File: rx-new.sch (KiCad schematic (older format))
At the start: 103 parts, among them J1 RF_IN, J2 PWR, J3 IQ_OUT, J4 4LO_IN, Q1 BC848, Q2 BC858, Q3 BC848, Q4 BC858, U1 TPS79101DBVREP, U2 SN74CBT3253, U3 AD797, U4 AD797, U5 NC7SZ00M5X, U6 OPA1662, U7 74AUP1G74, U8 74AUP1G74

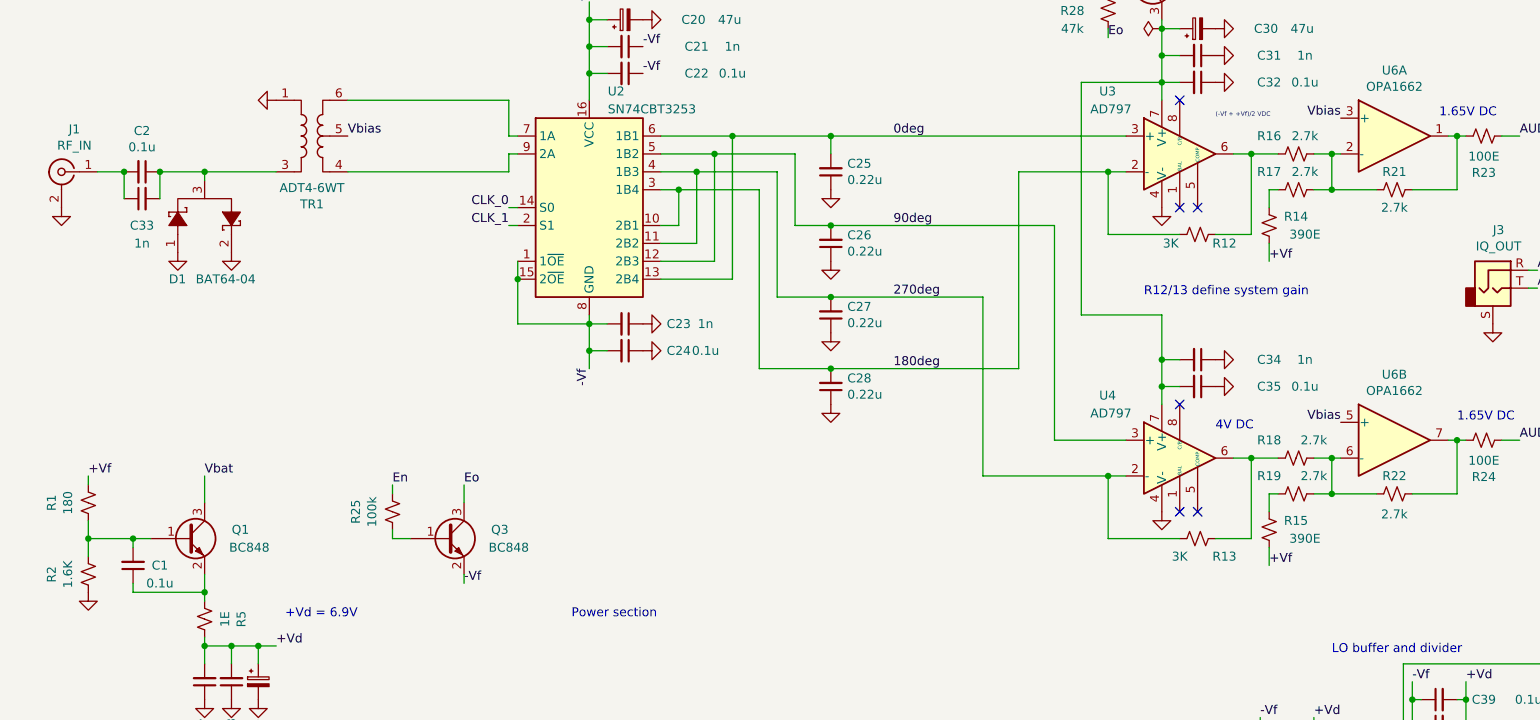
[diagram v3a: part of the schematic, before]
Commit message: Reworked voltages and opamps resistors
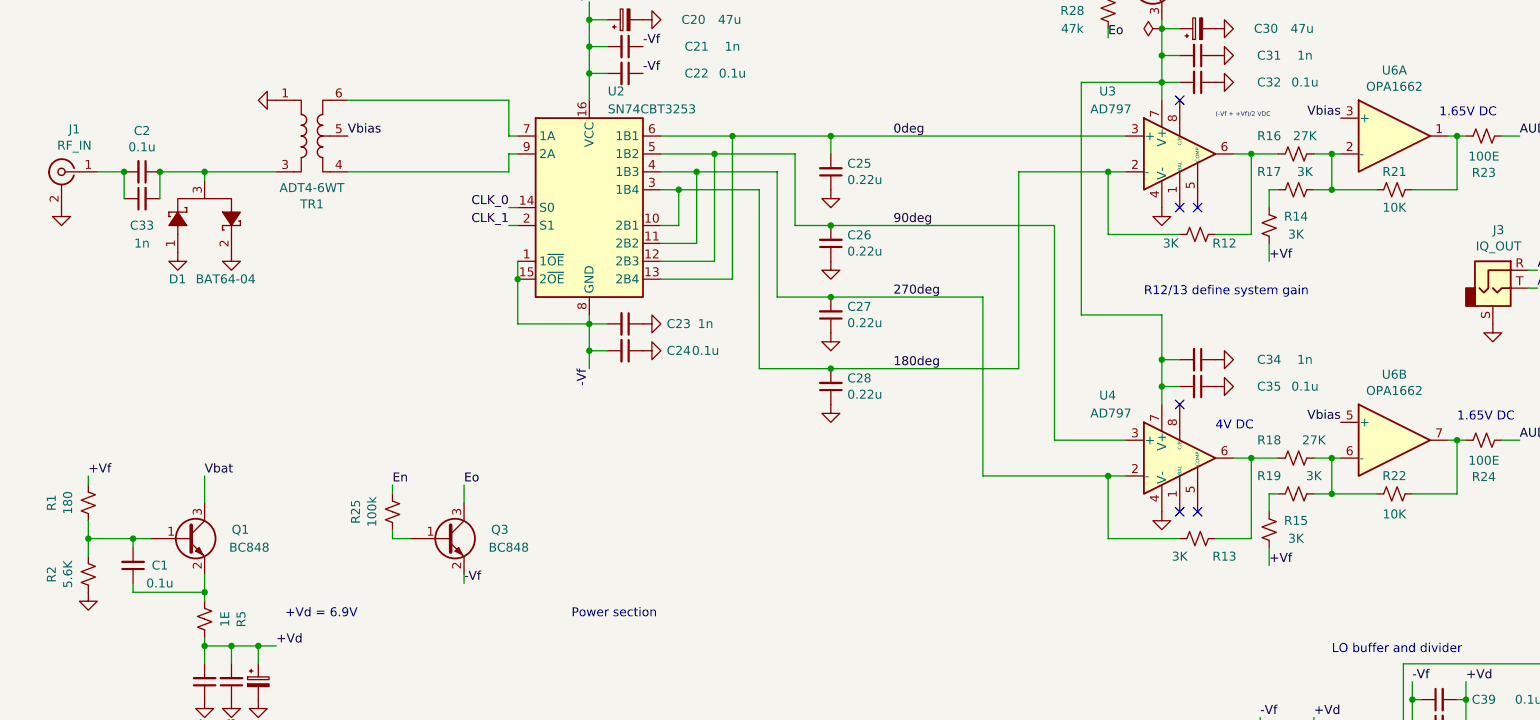
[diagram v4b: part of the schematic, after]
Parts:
- R14, R15: value 390E -> 3K
- R16, R18: value 2.7k -> 27K
- R17, R19: value 2.7k -> 3K
- R2: value 1.6K -> 5.6K
- R21, R22: value 2.7k -> 10K
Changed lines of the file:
@@
 Sheet 1 1
 Title "YO6SSW receiver v2"
-Date "2020-11-13"
-Rev "0.2"
+Date "2020-11-17"
+Rev "0.3"
 Comp "Frédéric Boes, Adrian Scripcă"
 Comment1 ""
@@
 P 1150 4100
 F 0 "R2" V 945 4100 50  0000 C CNN
-F 1 "1.6K" V 1036 4100 50  0000 C CNN
+F 1 "5.6K" V 1036 4100 50  0000 C CNN
 F 2 "Resistor_SMD:R_0805_2012Metric_Pad1.15x1.40mm_HandSolder" H 1150 4100 50  0001 C CNN
 F 3 "~" H 1150 4100 50  0001 C CNN
@@
 P 7900 1750
 F 0 "R16" V 8000 1900 50  0000 C CNN
-F 1 "2.7k" V 8000 1700 50  0000 C CNN
+F 1 "27K" V 8000 1700 50  0000 C CNN
 F 2 "Resistor_SMD:R_0805_2012Metric_Pad1.15x1.40mm_HandSolder" H 7900 1750 50  0001 C CNN
 F 3 "~" H 7900 1750 50  0001 C CNN
@@
 P 7900 1950
 F 0 "R17" V 8000 2100 50  0000 C CNN
-F 1 "2.7k" V 8000 1900 50  0000 C CNN
+F 1 "3K" V 8000 1900 50  0000 C CNN
 F 2 "Resistor_SMD:R_0805_2012Metric_Pad1.15x1.40mm_HandSolder" H 7900 1950 50  0001 C CNN
 F 3 "~" H 7900 1950 50  0001 C CNN
@@
 P 8450 1950
 F 0 "R21" V 8550 1950 50  0000 C CNN
-F 1 "2.7k" V 8350 1950 50  0000 C CNN
+F 1 "10K" V 8350 1950 50  0000 C CNN
 F 2 "Resistor_SMD:R_0805_2012Metric_Pad1.15x1.40mm_HandSolder" H 8450 1950 50  0001 C CNN
 F 3 "~" H 8450 1950 50  0001 C CNN
@@
 P 7750 2150
 F 0 "R14" H 7600 2100 50  0000 C CNN
-F 1 "390E" H 7550 2200 50  0000 C CNN
+F 1 "3K" H 7600 2200 50  0000 C CNN
 F 2 "Resistor_SMD:R_0805_2012Metric_Pad1.15x1.40mm_HandSolder" H 7750 2150 50  0001 C CNN
 F 3 "~" H 7750 2150 50  0001 C CNN
@@
 P 7900 3450
 F 0 "R18" V 8000 3600 50  0000 C CNN
-F 1 "2.7k" V 8000 3350 50  0000 C CNN
+F 1 "27K" V 8000 3350 50  0000 C CNN
 F 2 "Resistor_SMD:R_0805_2012Metric_Pad1.15x1.40mm_HandSolder" H 7900 3450 50  0001 C CNN
 F 3 "~" H 7900 3450 50  0001 C CNN
@@
 P 7900 3650
 F 0 "R19" V 8000 3800 50  0000 C CNN
-F 1 "2.7k" V 8000 3550 50  0000 C CNN
+F 1 "3K" V 8000 3550 50  0000 C CNN
 F 2 "Resistor_SMD:R_0805_2012Metric_Pad1.15x1.40mm_HandSolder" H 7900 3650 50  0001 C CNN
 F 3 "~" H 7900 3650 50  0001 C CNN
@@
 P 8450 3650
 F 0 "R22" V 8550 3650 50  0000 C CNN
-F 1 "2.7k" V 8336 3650 50  0000 C CNN
+F 1 "10K" V 8336 3650 50  0000 C CNN
 F 2 "Resistor_SMD:R_0805_2012Metric_Pad1.15x1.40mm_HandSolder" H 8450 3650 50  0001 C CNN
 F 3 "~" H 8450 3650 50  0001 C CNN
@@
 P 7750 3850
 F 0 "R15" H 7600 3800 50  0000 C CNN
-F 1 "390E" H 7550 3900 50  0000 C CNN
+F 1 "3K" H 7600 3900 50  0000 C CNN
 F 2 "Resistor_SMD:R_0805_2012Metric_Pad1.15x1.40mm_HandSolder" H 7750 3850 50  0001 C CNN
 F 3 "~" H 7750 3850 50  0001 C CNN

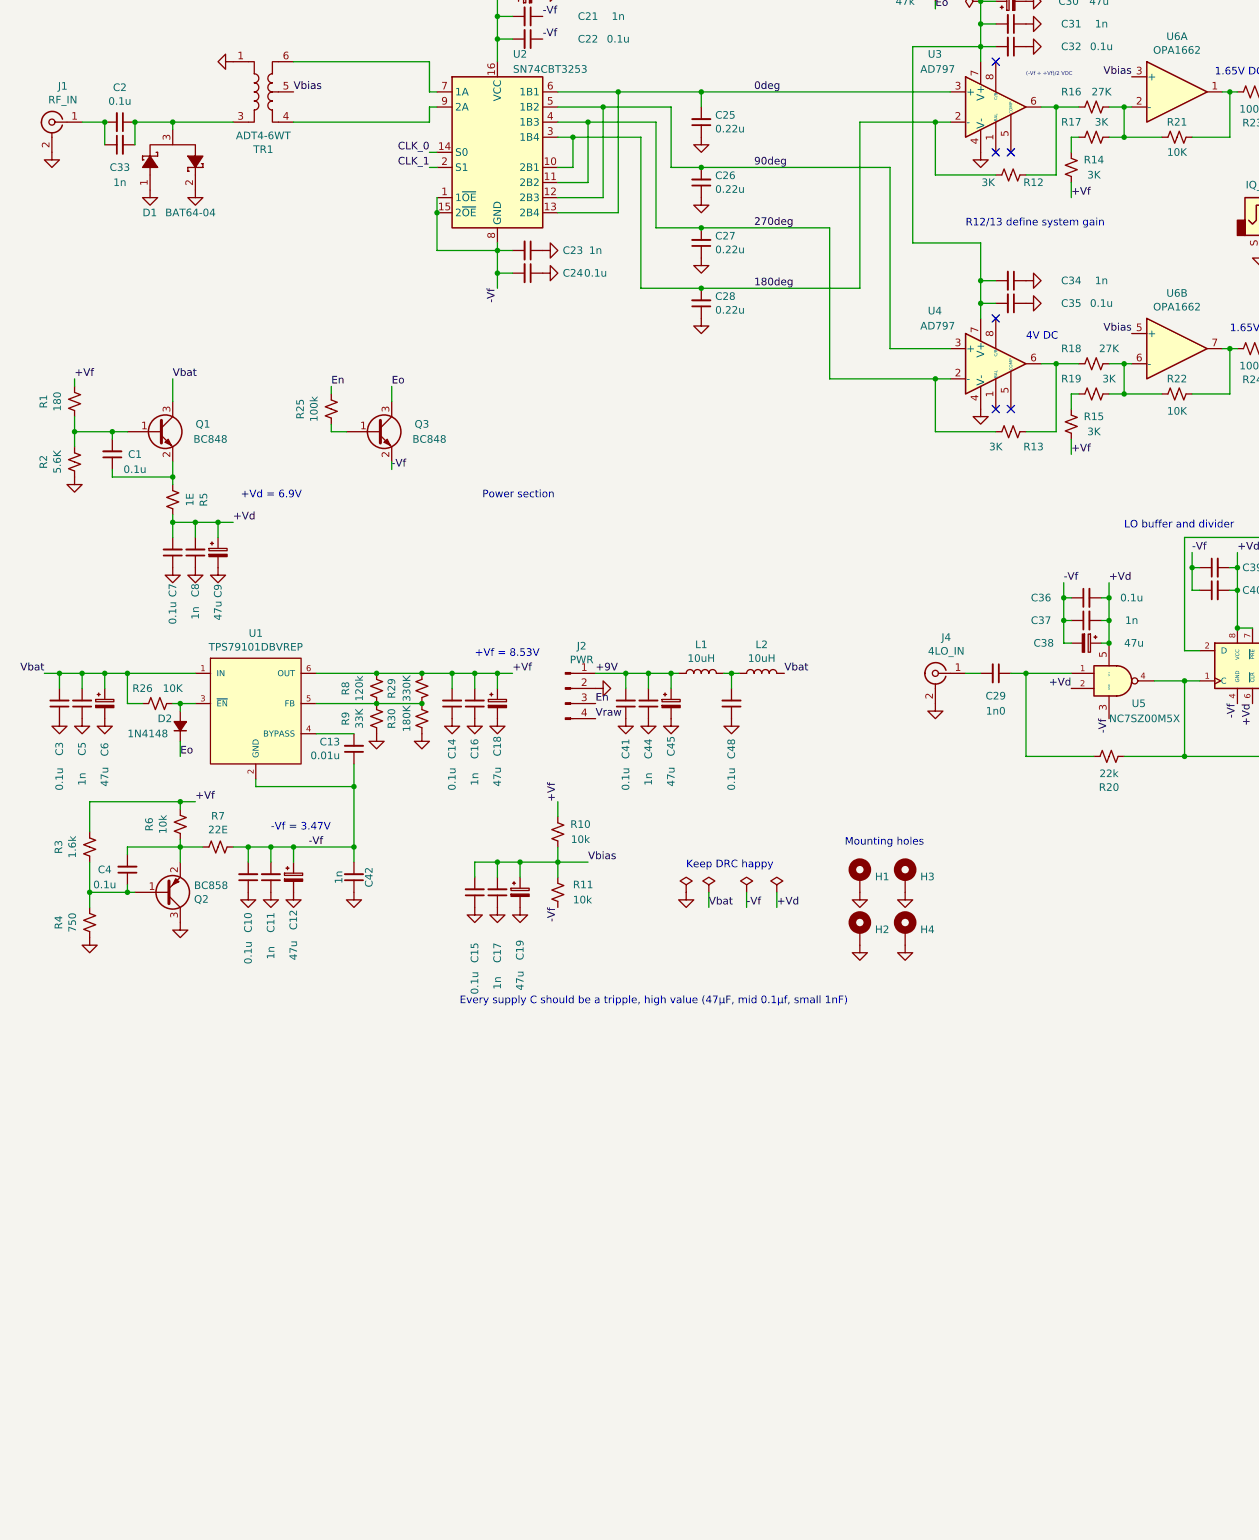
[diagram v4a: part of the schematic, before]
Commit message: Added selectable RX gain
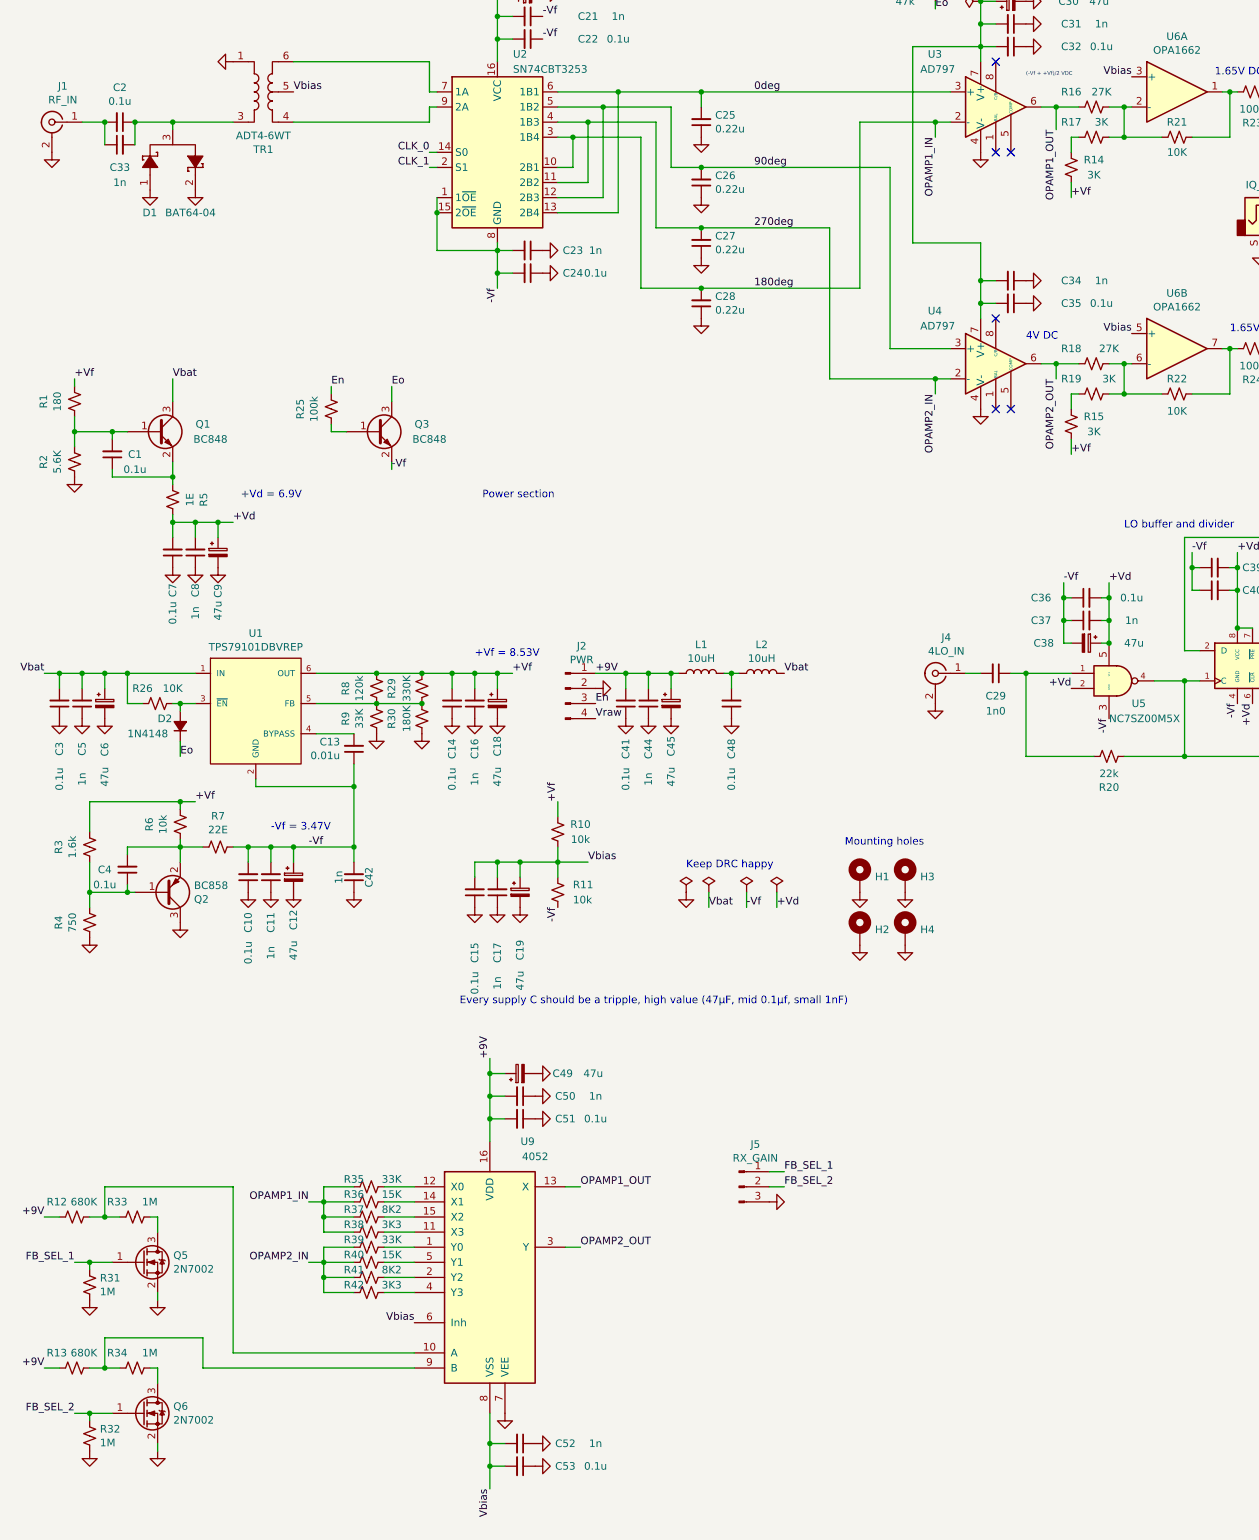
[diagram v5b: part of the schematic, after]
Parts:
- added C49: 47u, custom_library:CP_1210_3225Metric_Pad1.42x2.65mm_HandSolder, symbol Device:CP_Small
- added C50, C52: 1n, Capacitor_SMD:C_0805_2012Metric_Pad1.15x1.40mm_HandSolder, symbol Device:C_Small
- added C51, C53: 0.1u, Capacitor_SMD:C_0805_2012Metric_Pad1.15x1.40mm_HandSolder, symbol Device:C_Small
- added J5: RX_GAIN, symbol Connector:Conn_01x03_Male
- added Q5, Q6: 2N7002, Package_TO_SOT_SMD:SOT-23, symbol Transistor_FET:2N7002
- added R31, R32, R33, R34: 1M, Resistor_SMD:R_0805_2012Metric_Pad1.15x1.40mm_HandSolder, symbol Device:R_Small_US
- added R35, R39: 33K, Resistor_SMD:R_0805_2012Metric_Pad1.15x1.40mm_HandSolder, symbol Device:R_Small_US
- added R36, R40: 15K, Resistor_SMD:R_0805_2012Metric_Pad1.15x1.40mm_HandSolder, symbol Device:R_Small_US
- added R37, R41: 8K2, Resistor_SMD:R_0805_2012Metric_Pad1.15x1.40mm_HandSolder, symbol Device:R_Small_US
- added R38, R42: 3K3, Resistor_SMD:R_0805_2012Metric_Pad1.15x1.40mm_HandSolder, symbol Device:R_Small_US
- added U9: 4052, symbol 4xxx:4052
- R12, R13: value 3K -> 680K
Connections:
- net +9V: now also R12.2, R13.2, C49.1, C50.2, C51.2, U9.16 (VDD)
- net 180deg: now also R35.2, R36.2, R37.2, R38.2; no longer R12.1
- net 270deg: now also R39.2, R40.2, R41.2, R42.2; no longer R13.1
- net GND: now also C49.2, C50.1, C51.1, C52.1, C53.1, J5.3 (Pin_3), Q5.2 (S), Q6.2 (S), R31.2, R32.2, U9.7 (VEE)
- net Vbias: now also C52.2, C53.2, U9.6 (Inh), U9.8 (VSS)
- net OPAMP1_OUT: now reaches R16.1, U3.6
- net OPAMP1_OUT: now also U9.13 (X); no longer R12.2
- net OPAMP2_OUT: now reaches R18.1, U4.6
- net OPAMP2_OUT: now also U9.3 (Y); no longer R13.2
- new net: R39.1, U9.1 (Y0)
- new net: R12.1, R33.2, U9.10 (A)
- new net: R38.1, U9.11 (X3)
- new net: R35.1, U9.12 (X0)
- new net: R36.1, U9.14 (X1)
- new net: R37.1, U9.15 (X2)
- new net: R41.1, U9.2 (Y2)
- new net: R42.1, U9.4 (Y3)
- new net: R40.1, U9.5 (Y1)
- new net: R13.1, R34.2, U9.9 (B)
- new net: Q5.3 (D), R33.1
- new net: Q6.3 (D), R34.1
- new net FB_SEL_1: J5.1 (Pin_1), Q5.1 (G), R31.1
- new net FB_SEL_2: J5.2 (Pin_2), Q6.1 (G), R32.1
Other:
- note removed: "R12/13 define system gain"
